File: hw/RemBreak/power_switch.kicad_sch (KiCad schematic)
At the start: 39 parts, among them Q3 BC847, Q4 BC337, Q5 BC337, Q6 SiS415DNT, Q7 BC847, Q8 BC337, Q9 BC847, U3 BD48ExxG, U4 BD48ExxG, U5 L7805, U6 L7805, U7 XC6220B331MR, U8 MAX40200AUK

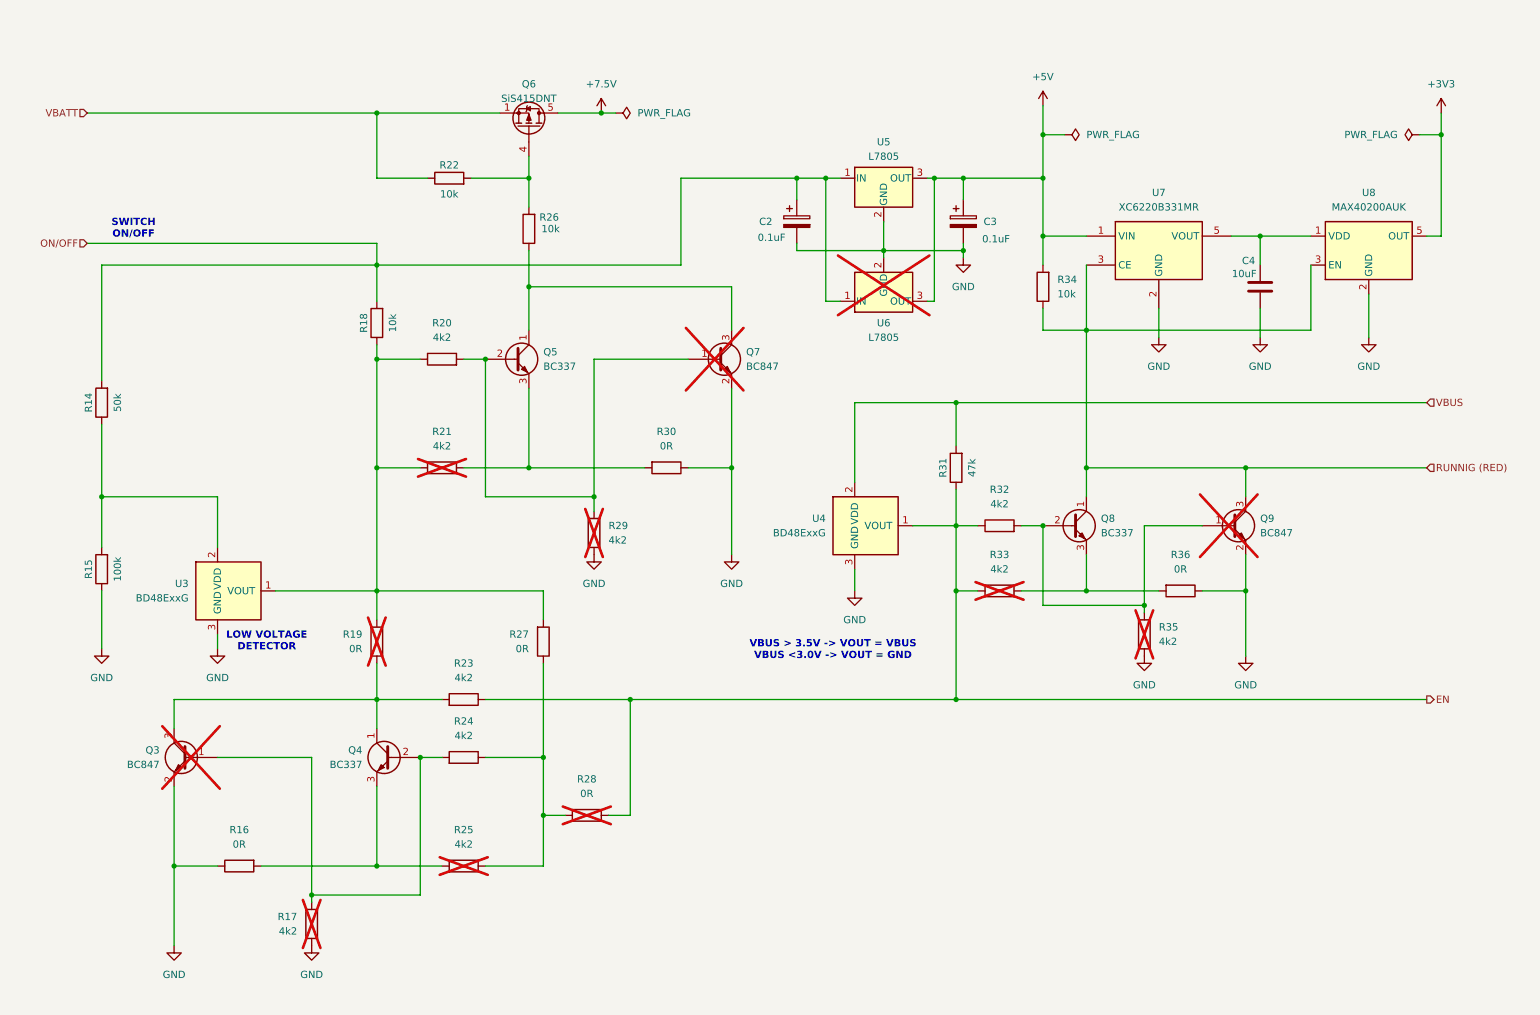
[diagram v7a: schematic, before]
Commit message: redrawing the schematics according the notes from the module design
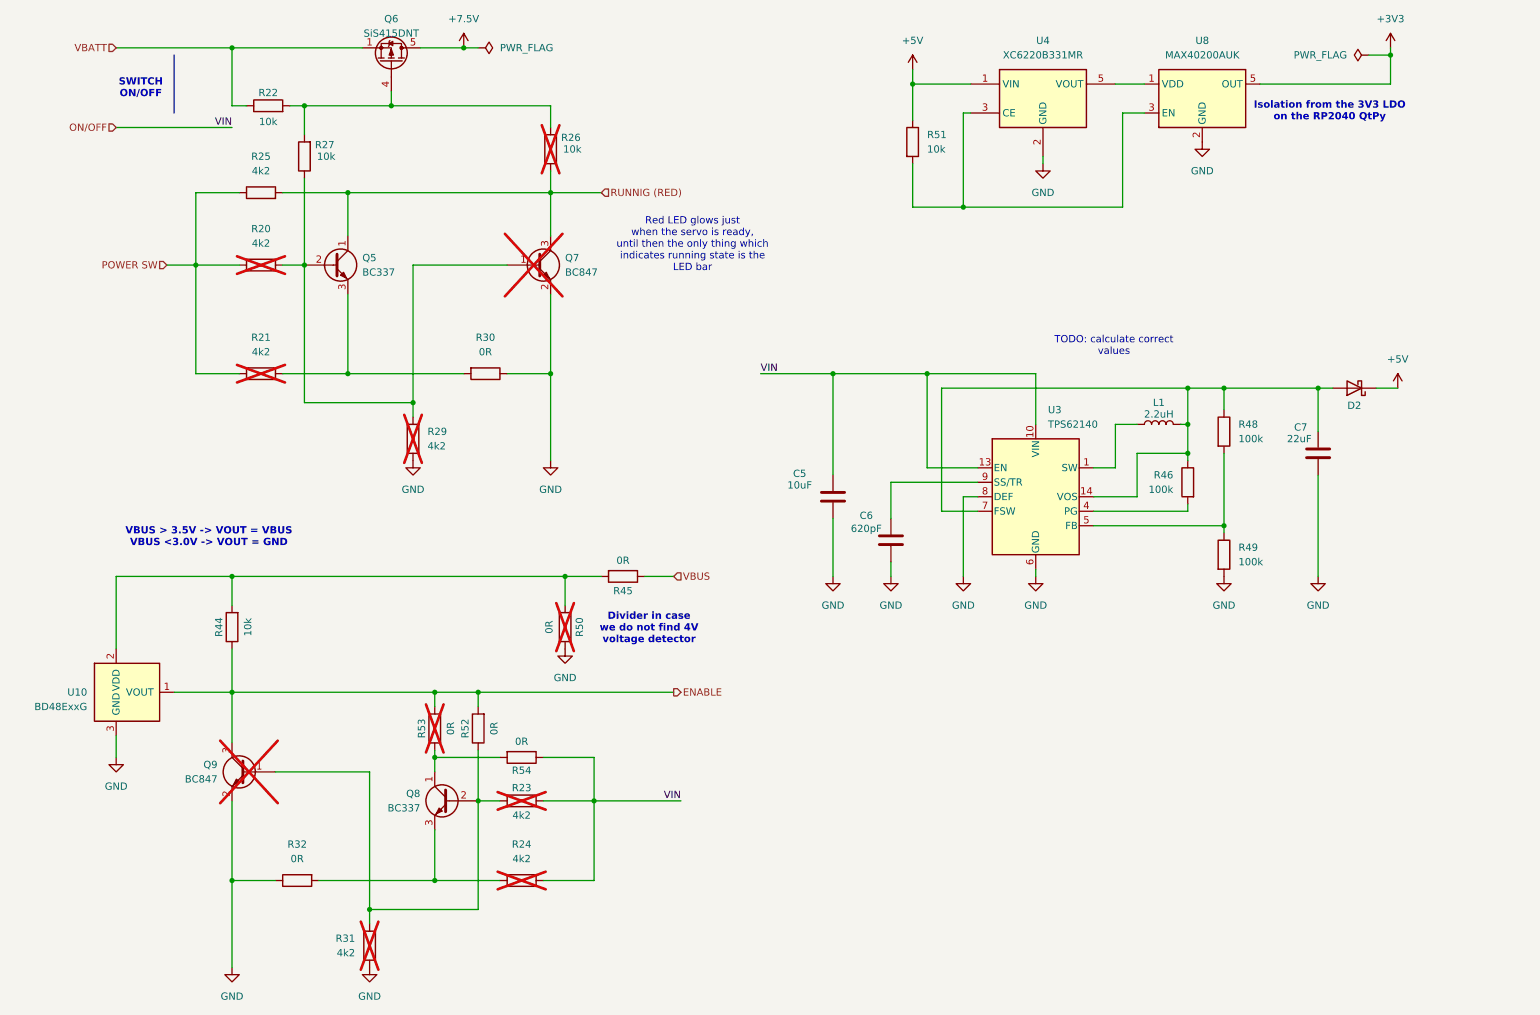
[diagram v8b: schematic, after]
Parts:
- removed C2, C3: 0.1uF, Capacitor_SMD:C_0805_2012Metric_Pad1.18x1.45mm_HandSolder, symbol Device:C_Polarized
- removed C4: 10uF, Capacitor_SMD:C_0805_2012Metric_Pad1.18x1.45mm_HandSolder, symbol Device:C
- removed Q3: BC847, Package_TO_SOT_SMD:SOT-23, symbol Transistor_BJT:BC847
- removed Q4: BC337, Package_TO_SOT_THT:TO-92_Inline, symbol Transistor_BJT:BC337
- removed R14: 50k, Resistor_SMD:R_0805_2012Metric_Pad1.20x1.40mm_HandSolder, symbol Device:R
- removed R15: 100k, Resistor_SMD:R_0805_2012Metric_Pad1.20x1.40mm_HandSolder, symbol Device:R
- removed R16, R19, R28, R36: 0R, Resistor_SMD:R_0805_2012Metric_Pad1.20x1.40mm_HandSolder, symbol Device:R
- removed R17, R33, R35: 4k2, Resistor_SMD:R_0805_2012Metric_Pad1.20x1.40mm_HandSolder, symbol Device:R
- removed R18, R34: 10k, Resistor_SMD:R_0805_2012Metric_Pad1.20x1.40mm_HandSolder, symbol Device:R
- removed U3, U4: BD48ExxG, Package_TO_SOT_SMD:SOT-23-5, symbol Power_Management:BD48ExxG
- removed U5: L7805, Package_TO_SOT_SMD:TO-263-2, symbol Regulator_Linear:L7805
- removed U6: L7805, Package_TO_SOT_THT:TO-220-3_Vertical, symbol Regulator_Linear:L7805
- removed U7: XC6220B331MR, Package_TO_SOT_SMD:SOT-23-5, symbol Regulator_Linear:XC6220B331MR
- added C5: 10uF, Capacitor_SMD:C_0805_2012Metric_Pad1.18x1.45mm_HandSolder, symbol Device:C
- added C6: 620pF, Capacitor_SMD:C_0805_2012Metric_Pad1.18x1.45mm_HandSolder, symbol Device:C
- added C7: 22uF, Capacitor_SMD:C_0805_2012Metric_Pad1.18x1.45mm_HandSolder, symbol Device:C
- added D2: D_Schottky, symbol Device:D_Schottky
- added L1: 2.2uH, symbol Device:L
- added R44, R51: 10k, Resistor_SMD:R_0805_2012Metric_Pad1.20x1.40mm_HandSolder, symbol Device:R
- added R45, R50, R52, R53, R54: 0R, Resistor_SMD:R_0805_2012Metric_Pad1.20x1.40mm_HandSolder, symbol Device:R
- added R46, R48, R49: 100k, Resistor_SMD:R_0805_2012Metric_Pad1.20x1.40mm_HandSolder, symbol Device:R
- added U10: BD48ExxG, Package_TO_SOT_SMD:SOT-23-5, symbol Power_Management:BD48ExxG
- added U3: TPS62140, Package_DFN_QFN:VQFN-16-1EP_3x3mm_P0.5mm_EP1.68x1.68mm_ThermalVias, symbol Regulator_Switching:TPS62140
- added U4: XC6220B331MR, Package_TO_SOT_SMD:SOT-23-5, symbol Regulator_Linear:XC6220B331MR
- R20, R23, R24, R26: now not fitted
- R25: now fitted
- R27: value 0R -> 10k
- R31: value 47k -> 4k2; now not fitted
- R32: value 4k2 -> 0R
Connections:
- net +5V: now also D2.1 (K), R51.1, U4.1 (VIN)
- net GND: now also R31.1, R32.1, C5.2, C6.2, C7.2, R49.2, R50.2, U10.3 (GND), U3.15 (GND), U3.16 (GND), U3.17 (GND), U3.6 (GND), U3.8 (DEF), U4.2 (GND)
- net ON/OFF: now also R23.1, R24.1, C5.1, R54.1, U3.10 (VIN), U3.11 (VIN), U3.12 (VIN), U3.13 (EN)
- net RUNNIG (RED): now also Q5.1 (C), Q7.3 (C), R25.2, R26.1; no longer Q8.1 (C), Q9.3 (C), U8.3 (EN)
- net VBUS: now also R45.1; no longer R31.2
- net at Q5.2 (B), Q7.1 (B), R20.2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: now also R27.1
- net at Q8.2 (B), Q9.1 (B): now also R23.2, R31.2, R52.1; no longer R32.2
- net at U8.1 (VDD): now also U4.5 (VOUT)
- net POWER SW: now reaches R20.1, R21.1
- net POWER SW: now also R25.1; no longer R27.2
- net at Q6.4 (G), R22.2, R26.2: now also R27.2
- net at R24.2: now also Q8.3 (E), R32.2
- removed net EN: R23.1, R31.1, R32.1
- new net: Q8.1 (C), R53.1, R54.2
- new net: R51.2, U4.3 (CE), U8.3 (EN)
- new net: L1.1, U3.1 (SW), U3.2 (SW), U3.3 (SW)
- new net: C7.1, D2.2 (A), L1.2, R46.1, R48.1, U3.14 (VOS), U3.7 (FSW)
- new net: R46.2, U3.4 (PG)
- new net: R48.2, R49.1, U3.5 (FB)
- new net: C6.1, U3.9 (SS/TR)
- new net: R44.2, R45.2, R50.1, U10.2 (VDD)
- new net ENABLE: Q9.3 (C), R44.1, R52.2, R53.2, U10.1 (VOUT)
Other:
- note added: "Divider in case we do not find 4V voltage detector"
- note added: "Isolation from the 3V3 LDO on the RP2040 QtPy"
- note added: "Red LED glows just when the servo is ready, until then the only thing which indicates running state is the LED bar"
- note added: "TODO: calculate correct values"
- note removed: "LOW VOLTAGE DETECTOR"
- moved on the sheet: Q5, Q6, Q7, R21, R22, R29, R30, U8
